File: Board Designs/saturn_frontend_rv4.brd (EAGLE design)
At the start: 95.6 x 73.6 mm, 44 parts

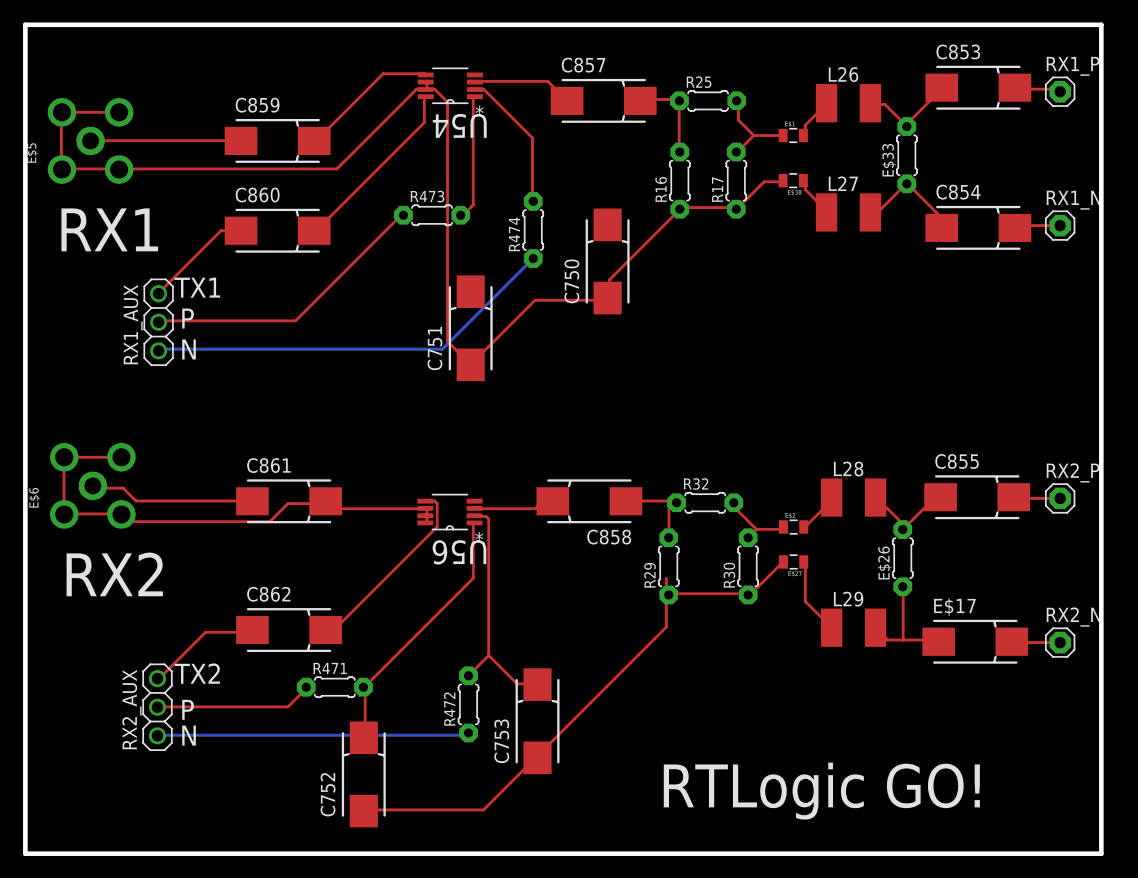
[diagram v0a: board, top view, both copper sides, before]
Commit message: Moved board designs to a seperate directory to keep SPICE/ clean
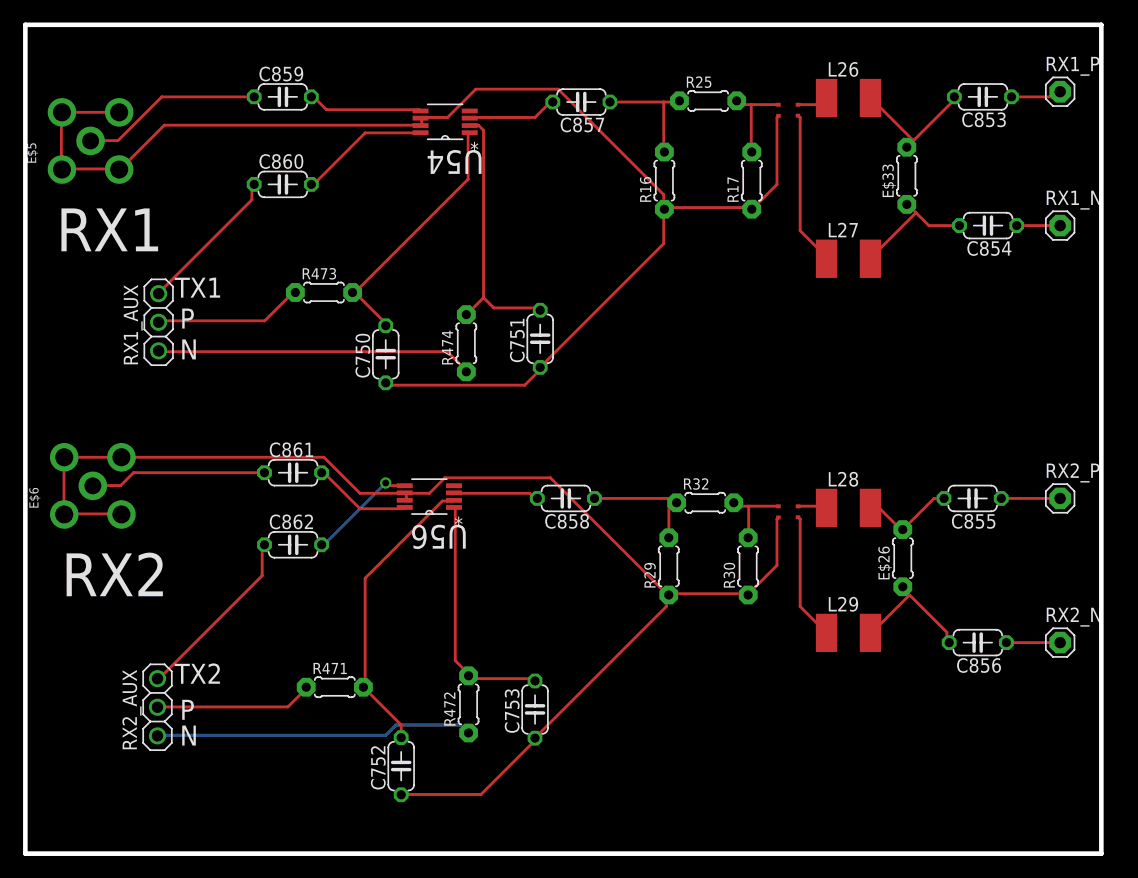
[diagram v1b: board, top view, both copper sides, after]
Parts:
- removed E$17: 100 pF, adafruit:085CS_1AR
- removed E$27, E$38: (no value), 0805:0805
- added C856: 100 pF, adafruit:C050-024X044
- C750, C751, C752, C753, C853, C854, C855, C857, C858, C859, C860, C861: device adafruit:085CS_1AR -> adafruit:C050-024X044
- C862: value 100 pF -> (none); device adafruit:085CS_1AR -> adafruit:C050-024X044
- E$1, E$2: device 0805:0805 -> cody_custom_library:BALUN_LOGICALS
- moved C750 21.4 mm to (41.6, 56.2)
- moved R473 11.8 mm to (36.1, 61.7)
- moved R474 11.7 mm to (48.8, 57.2)
- moved C862 7.58 mm to (33.4, 39.3)
- moved C751 6.24 mm to (55.3, 57.6)
- moved C860 4.14 mm to (32.5, 71.3)
- moved L27 4.11 mm to (82.7, 64.7)
- moved C859 3.94 mm to (32.5, 79.1)
- moved C752 3.40 mm to (43.0, 19.7)
- moved U54 3.23 mm to (46.9, 76.9)
- moved C861 2.56 mm to (33.4, 45.7)
- moved U56 2.29 mm to (45.5, 43.6)
- moved E$1 2.15 mm to (76.4, 77.3)
- moved C858 2.10 mm to (57.6, 43.4)
- moved C857 1.98 mm to (59.0, 78.6), turned to 180 degrees
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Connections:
- removed net J11: C750.-, C751.-, E$38.2, E$5.GND1, E$5.GND2, E$5.GND3, E$5.GND4, R16.1, R17.1, U54.6, U54.7
- removed net J12: C752.-, C753.-, E$27.2, R29.1, R30.1
- removed net S$11: C854.+, RX1_N.1
- removed net S$17: C855.+, RX2_P.1
- removed net S$21: E$17.+, RX2_N.1
- removed net S$22: R473.2, U54.1
- removed net S$26: C857.+, R16.2, R25.1
- new net S$38: C859.1, E$5.ANTENNA
- new net S$46: C752.1, C753.1, E$2.2, E$6.GND1, E$6.GND2, E$6.GND3, E$6.GND4, R29.1, R30.1, U56.6, U56.7
- new net S$47: C856.1, RX2_N.1
- new net S$49: R472.1, RX2_AUX.1
- net S$1: now also E$2.1, R30.2, R32.2; no longer C853.+, RX1_P.1
- net S$10: now also C857.1, R16.2, R25.1; no longer E$2.1, R30.2, R32.2
- net S$12: now also E$1.1, R17.2, R25.2; no longer C853.-, E$33.2, L26.2
- net S$14: now also E$1.4, L26.1; no longer E$2.2, L28.1
- net S$16: now also E$1.3, L27.1; no longer C859.+, U54.5
- net S$18: now also C853.2, E$33.2, L26.2; no longer C860.+, U54.8
- net S$19: now also C854.2, E$33.1, L27.2; no longer C858.+
- net S$2: now also E$2.4, L28.1; no longer C751.+
- net S$23: now also C853.1, RX1_P.1; no longer R474.2, U54.2
- net S$24: now also C854.1, RX1_N.1; no longer C861.+, E$6.GND1, E$6.GND2, E$6.GND3, E$6.GND4, U56.6, U56.7, U56.8
- net S$25: now also R473.1, RX1_AUX.2; no longer R474.1, RX1_AUX.1
- net S$27: now also C750.2, R473.2, U54.1; no longer E$1.1, R17.2, R25.2
- net S$28: now also C751.2, R474.2, U54.2; no longer E$1.2, L26.1
- net S$29: now also R474.1, RX1_AUX.1; no longer E$38.1, L27.1
- net S$3: now also C858.1, R29.2, R32.1; no longer C750.+
- net S$32: now also R471.1, RX2_AUX.2; no longer C862.-, RX2_AUX.3
- net S$33: now also C752.2, R471.2, U56.2; no longer R471.1, RX2_AUX.2
- net S$34: now also C753.2, R472.2, U56.1; no longer R472.1, RX2_AUX.1
- net S$35: now also C861.1, E$6.ANTENNA; no longer C862.+, U56.5
- net S$36: now also C862.1, RX2_AUX.3; no longer C861.-, E$6.ANTENNA
- net S$37: now also C860.1, RX1_AUX.3; no longer C857.-, U54.3
- net S$39: now also C859.2, U54.5; no longer U56.3
- net S$40: now also C860.2, U54.8; no longer C752.+, R471.2, U56.1
- net S$41: now also C862.2, U56.5; no longer C753.+, R472.2, U56.2
- net S$42: now also C861.2, U56.8; no longer C858.-, R29.2, R32.1
- net S$43: now also C858.2, U56.3; no longer E$27.1, L29.1
- net S$44: now also C857.2, U54.3; no longer C855.-, E$26.2, L28.2
- net S$45: now also C750.1, C751.1, E$1.2, E$5.GND1, E$5.GND2, E$5.GND3, E$5.GND4, R16.1, R17.1, U54.6, U54.7; no longer E$17.-, E$26.1, L29.2
- net S$5: now also C855.2, E$26.2, L28.2; no longer C859.-, E$5.ANTENNA
- net S$6: now also C855.1, RX2_P.1; no longer C854.-, E$33.1, L27.2
- net S$7: now also C856.2, E$26.1, L29.2; no longer C860.-, RX1_AUX.3
- net S$8: now also E$2.3, L29.1; no longer R473.1, RX1_AUX.2
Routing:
- net S$46: track 0.00 -> 117.7 mm
- net S$45: track 10.8 -> 122.8 mm
- net J11: track 108.5 -> 0.00 mm
- net S$48: track 0.00 -> 95.6 mm
- net J12: track 50.0 -> 0.00 mm
- net S$24: track 45.3 -> 3.86 mm
- net S$49: track 0.00 -> 28.3 mm
- net S$29: track 3.68 -> 28.2 mm
- net S$25: track 36.7 -> 13.3 mm
- net S$28: track 3.81 -> 24.0 mm
- net S$38: track 0.00 -> 16.1 mm
- net S$8: track 25.7 -> 11.3 mm
- net S$27: track 8.47 -> 22.8 mm
- net S$33: track 14.0 -> 26.4 mm
- net S$40: track 23.4 -> 11.6 mm
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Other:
- board text added: "Saturn Front End MK4"
- board text removed: "RTLogic GO!"
